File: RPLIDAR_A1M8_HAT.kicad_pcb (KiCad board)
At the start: 2 copper layers, 70.2 x 96.7 mm, 5 parts

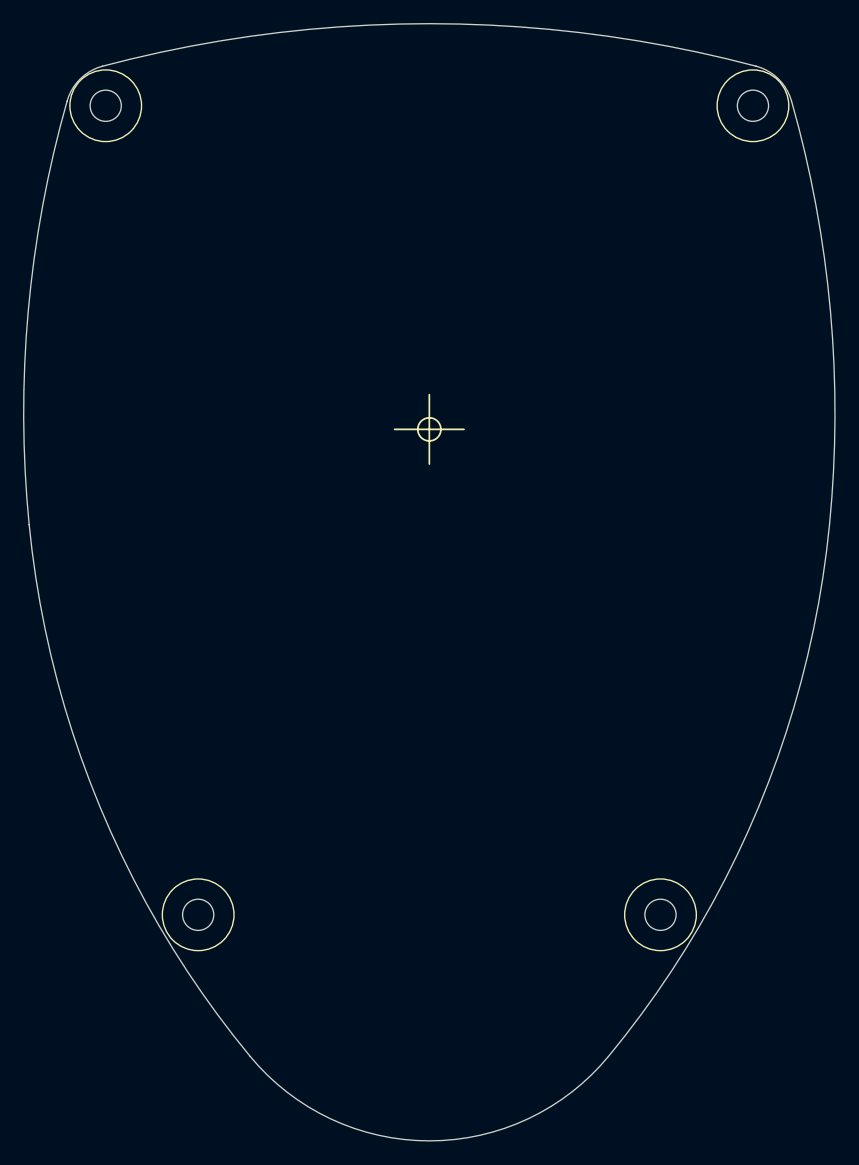
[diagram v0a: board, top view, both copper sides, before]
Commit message: chore: convert project to KiCad v10
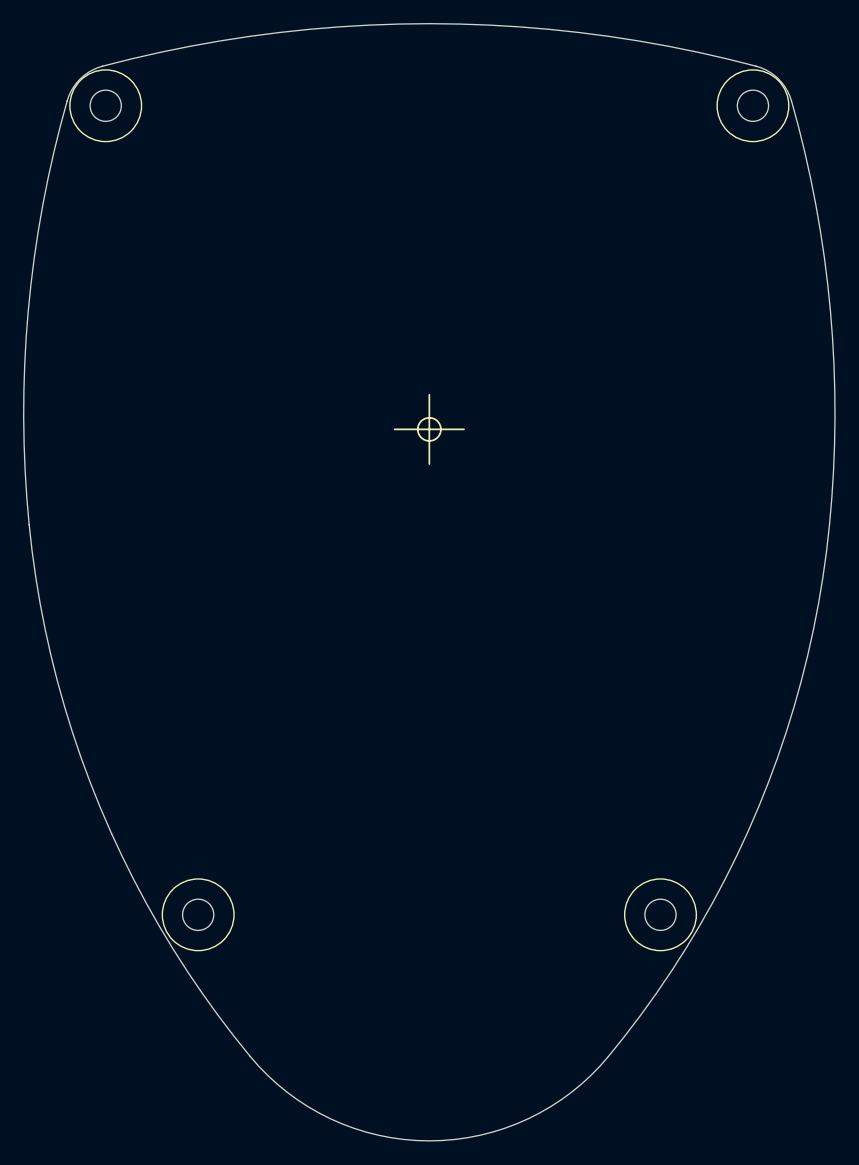
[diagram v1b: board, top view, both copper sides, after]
